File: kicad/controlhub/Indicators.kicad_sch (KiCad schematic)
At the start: 4 parts

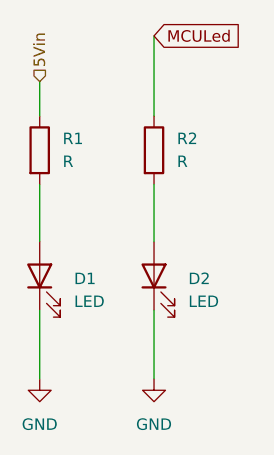
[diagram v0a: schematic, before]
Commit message: removed uneccesary schematics and worked on proper wiring
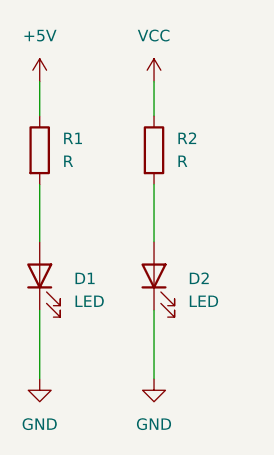
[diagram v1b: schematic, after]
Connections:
- net 5Vin renamed +5V
- net MCULed renamed VCC
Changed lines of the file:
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@@
 	(wire
 		(pts
-			(xy 127 50.8) (xy 127 59.69)
+			(xy 127 55.88) (xy 127 59.69)
 		)
 		(stroke
@@
 		)
 	)
-	(global_label "MCULed"
-		(shape input)
-		(at 127 50.8 0)
-		(fields_autoplaced yes)
-		(effects
-			(font
-				(size 1.27 1.27)
-			)
-			(justify left)
-		)
-		(property "Intersheetrefs" "${INTERSHEET_REFS}"
-			(at 136.6486 50.8 0)
-			(effects
-				(font
-					(size 1.27 1.27)
-				)
-				(justify left)
-				(hide yes)
-			)
-		)
-	)
-	(hierarchical_label "5Vin"
-		(shape input)
-		(at 114.3 55.88 90)
-		(effects
-			(font
-				(size 1.27 1.27)
-			)
-			(justify left)
-		)
-	)
 	(symbol
 		(lib_id "Device:LED")
@@
 					(unit 1)
 				)
+			)
+		)
+	)
+	(symbol
+		(lib_id "power:VCC")
+		(at 127 55.88 0)
+		(unit 1)
+		(exclude_from_sim no)
+		(in_bom yes)
+		(on_board yes)
+		(dnp no)
+		(fields_autoplaced yes)
+		(property "Reference" "#PWR027"
+			(at 127 59.69 0)
+			(effects
+				(font
+					(size 1.27 1.27)
+				)
+				(hide yes)
+			)
+		)
+		(property "Value" "VCC"
+			(at 127 50.8 0)
+			(effects
+				(font
+					(size 1.27 1.27)
+				)
+			)
+		)
+		(property "Footprint" ""
+			(at 127 55.88 0)
+			(effects
+				(font
+					(size 1.27 1.27)
+				)
+				(hide yes)
+			)
+		)
+		(property "Datasheet" ""
+			(at 127 55.88 0)
+			(effects
+				(font
+					(size 1.27 1.27)
+				)
+				(hide yes)
+			)
+		)
+		(property "Description" "Power symbol creates a global label with name \"VCC\""
+			(at 127 55.88 0)
+			(effects
+				(font
+					(size 1.27 1.27)
+				)
+				(hide yes)
+			)
+		)
+		(pin "1"
+		)
+		(instances
+			(project ""
+				(path "/78f9b8b9-94ed-46bb-ab2b-797c156bf665/14ea8e61-8e65-415a-aef4-444b25cd536e"
+					(reference "#PWR027")
+					(unit 1)
+				)
+			)
+		)
+	)
+	(symbol
+		(lib_id "power:+5V")
+		(at 114.3 55.88 0)
+		(unit 1)
+		(exclude_from_sim no)
+		(in_bom yes)
+		(on_board yes)
+		(dnp no)
+		(fields_autoplaced yes)
+		(property "Reference" "#PWR026"
+			(at 114.3 59.69 0)
+			(effects
+				(font
+					(size 1.27 1.27)
+				)
+				(hide yes)
+			)
+		)
+		(property "Value" "+5V"
+			(at 114.3 50.8 0)
+			(effects
+				(font
+					(size 1.27 1.27)
+				)
+			)
+		)
+		(property "Footprint" ""
+			(at 114.3 55.88 0)
+			(effects
+				(font
+					(size 1.27 1.27)
+				)
+				(hide yes)
+			)
+		)
+		(property "Datasheet" ""
+			(at 114.3 55.88 0)
+			(effects
+				(font
+					(size 1.27 1.27)
+				)
+				(hide yes)
+			)
+		)
+		(property "Description" "Power symbol creates a global label with name \"+5V\""
+			(at 114.3 55.88 0)
+			(effects
+				(font
+					(size 1.27 1.27)
+				)
+				(hide yes)
+			)
+		)
+		(pin "1"
+		)
+		(instances
+			(project ""
+				(path "/78f9b8b9-94ed-46bb-ab2b-797c156bf665/14ea8e61-8e65-415a-aef4-444b25cd536e"
+					(reference "#PWR026")
+					(unit 1)
+				)
